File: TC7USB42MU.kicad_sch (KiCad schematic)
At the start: 5 parts

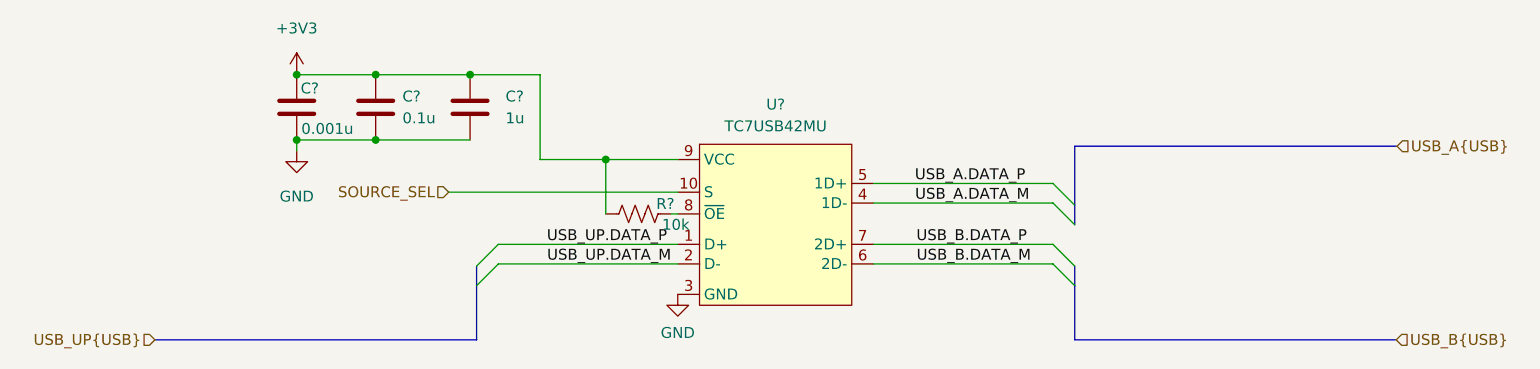
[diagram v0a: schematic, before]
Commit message: Adding 5v and 3v3 buck
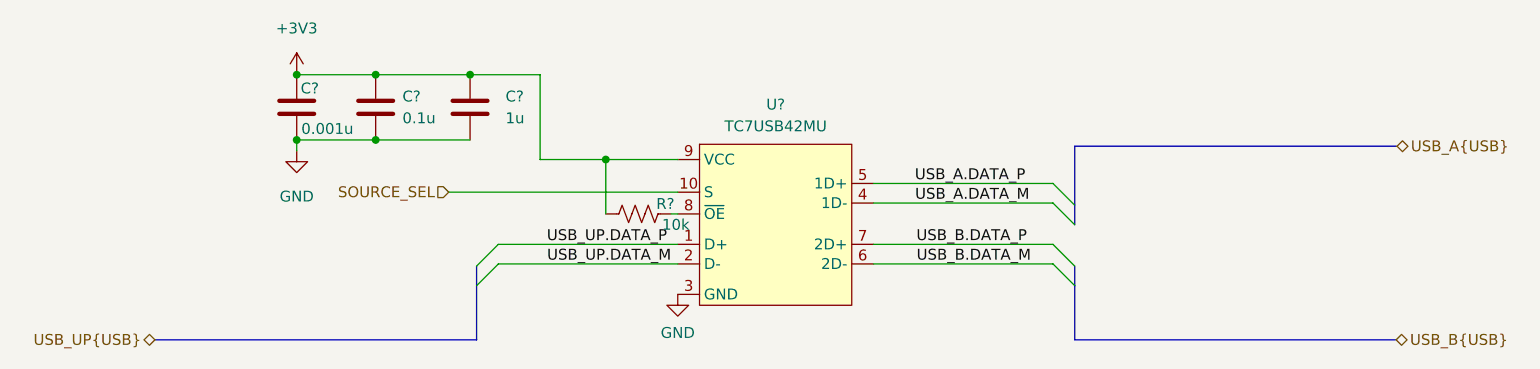
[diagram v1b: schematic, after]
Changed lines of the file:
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@@
     (effects (font (size 1.27 1.27)) (justify right))
   )
-  (hierarchical_label "USB_B{USB}" (shape input) (at 220.0148 104.9528 0)
+  (hierarchical_label "USB_B{USB}" (shape bidirectional) (at 220.0148 104.9528 0)
     (effects (font (size 1.27 1.27)) (justify left))
   )
-  (hierarchical_label "USB_A{USB}" (shape input) (at 220.1164 82.3468 0)
+  (hierarchical_label "USB_A{USB}" (shape bidirectional) (at 220.1164 82.3468 0)
     (effects (font (size 1.27 1.27)) (justify left))
   )
-  (hierarchical_label "USB_UP{USB}" (shape input) (at 75.057 104.9528 180)
+  (hierarchical_label "USB_UP{USB}" (shape bidirectional) (at 75.057 104.9528 180)
     (effects (font (size 1.27 1.27)) (justify right))
   )

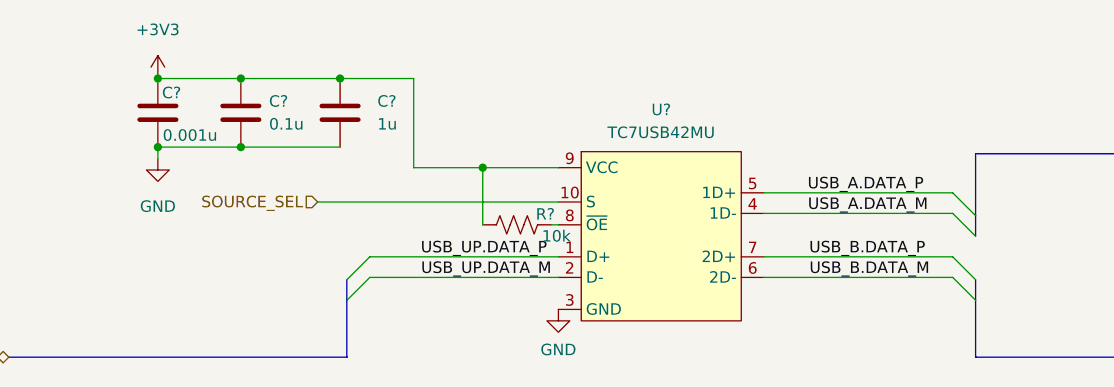
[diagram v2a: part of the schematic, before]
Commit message: Fixing ERC
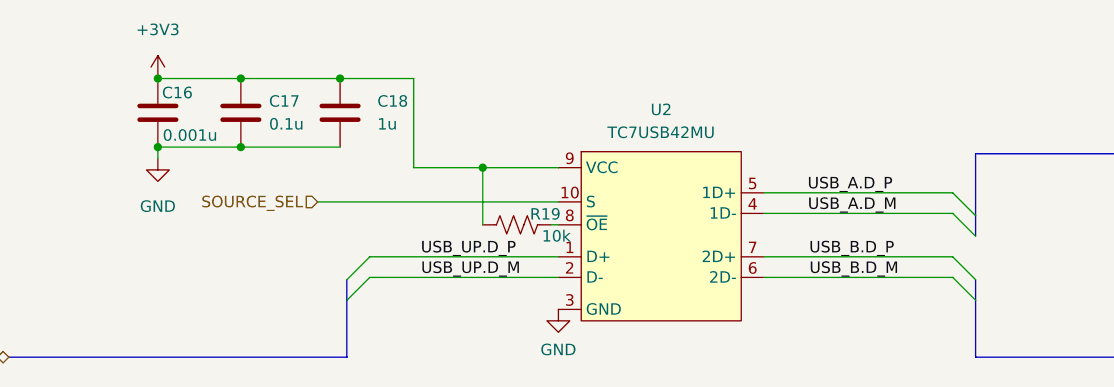
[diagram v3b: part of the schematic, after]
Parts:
- gave numbers to parts that had none: 5
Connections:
- net USB_A.DATA_M renamed USB_A.D_M
- net USB_A.DATA_P renamed USB_A.D_P
- net USB_B.DATA_M renamed USB_B.D_M
- net USB_B.DATA_P renamed USB_B.D_P
- net USB_UP.DATA_M renamed USB_UP.D_M
- net USB_UP.DATA_P renamed USB_UP.D_P
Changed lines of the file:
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@@
     (stroke (width 0) (type default) (color 0 0 0 0))
   )
-  (label "USB_UP.DATA_P" (at 120.8278 93.8022 0)
+  (label "USB_UP.D_P" (at 120.8278 93.8022 0)
     (effects (font (size 1.27 1.27)) (justify left bottom))
   )
-  (label "USB_B.DATA_M" (at 164.0078 96.0882 0)
+  (label "USB_B.D_M" (at 164.0078 96.0882 0)
     (effects (font (size 1.27 1.27)) (justify left bottom))
   )
-  (label "USB_A.DATA_M" (at 163.83 88.9762 0)
+  (label "USB_A.D_M" (at 163.83 88.9762 0)
     (effects (font (size 1.27 1.27)) (justify left bottom))
   )
-  (label "USB_UP.DATA_M" (at 120.8532 96.0882 0)
+  (label "USB_UP.D_M" (at 120.8532 96.0882 0)
     (effects (font (size 1.27 1.27)) (justify left bottom))
   )
-  (label "USB_B.DATA_P" (at 163.9824 93.8022 0)
+  (label "USB_B.D_P" (at 163.9824 93.8022 0)
     (effects (font (size 1.27 1.27)) (justify left bottom))
   )
-  (label "USB_A.DATA_P" (at 163.8046 86.6902 0)
+  (label "USB_A.D_P" (at 163.8046 86.6902 0)
     (effects (font (size 1.27 1.27)) (justify left bottom))
   )
@@
   (symbol (lib_id "Device:C") (at 100.838 77.8002 0) (unit 1)
     (in_bom yes) (on_board yes) (fields_autoplaced)
-    (property "Reference" "C?" (id 0) (at 103.9622 76.5301 0)
+    (property "Reference" "C17" (id 0) (at 103.9622 76.5301 0)
       (effects (font (size 1.27 1.27)) (justify left))
     )
@@
   (symbol (lib_id "power:GND") (at 136.1186 99.6442 0) (unit 1)
     (in_bom yes) (on_board yes) (fields_autoplaced)
-    (property "Reference" "#PWR?" (id 0) (at 136.1186 105.9942 0)
+    (property "Reference" "#PWR031" (id 0) (at 136.1186 105.9942 0)
       (effects (font (size 1.27 1.27)) hide)
     )
@@
   (symbol (lib_id "Misic:TC7USB42MU") (at 147.8026 93.8022 0) (unit 1)
     (in_bom yes) (on_board yes) (fields_autoplaced)
-    (property "Reference" "U?" (id 0) (at 147.5486 77.47 0))
+    (property "Reference" "U2" (id 0) (at 147.5486 77.47 0))
     (property "Value" "TC7USB42MU" (id 1) (at 147.5486 80.01 0))
     (property "Footprint" "" (id 2) (at 147.2946 94.0562 0)
@@
   (symbol (lib_id "Device:C") (at 111.8616 77.8002 0) (unit 1)
     (in_bom yes) (on_board yes) (fields_autoplaced)
-    (property "Reference" "C?" (id 0) (at 116.0018 76.5301 0)
+    (property "Reference" "C18" (id 0) (at 116.0018 76.5301 0)
       (effects (font (size 1.27 1.27)) (justify left))
     )
@@
   (symbol (lib_id "Device:R_US") (at 131.5212 90.2462 90) (unit 1)
     (in_bom yes) (on_board yes)
-    (property "Reference" "R?" (id 0) (at 134.6708 89.0778 90))
+    (property "Reference" "R19" (id 0) (at 134.6708 89.0778 90))
     (property "Value" "10k" (id 1) (at 135.89 91.5162 90))
     (property "Footprint" "" (id 2) (at 131.7752 89.2302 90)
@@
   (symbol (lib_id "power:GND") (at 91.6178 82.8802 0) (unit 1)
     (in_bom yes) (on_board yes) (fields_autoplaced)
-    (property "Reference" "#PWR?" (id 0) (at 91.6178 89.2302 0)
+    (property "Reference" "#PWR030" (id 0) (at 91.6178 89.2302 0)
       (effects (font (size 1.27 1.27)) hide)
     )
@@
   (symbol (lib_id "power:+3V3") (at 91.6178 73.9902 0) (unit 1)
     (in_bom yes) (on_board yes) (fields_autoplaced)
-    (property "Reference" "#PWR?" (id 0) (at 91.6178 77.8002 0)
+    (property "Reference" "#PWR029" (id 0) (at 91.6178 77.8002 0)
       (effects (font (size 1.27 1.27)) hide)
     )
@@
   (symbol (lib_id "Device:C") (at 91.6178 77.8002 0) (unit 1)
     (in_bom yes) (on_board yes)
-    (property "Reference" "C?" (id 0) (at 92.075 75.5904 0)
+    (property "Reference" "C16" (id 0) (at 92.075 75.5904 0)
       (effects (font (size 1.27 1.27)) (justify left))
     )

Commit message: Pushing what i have now
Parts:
- removed C16: 0.001u, symbol Device:C
- removed C17: 0.1u, symbol Device:C
- removed C18: 1u, symbol Device:C
- removed R19: 10k, symbol Device:R_US
- removed U2: TC7USB42MU, symbol Misic:TC7USB42MU
- added C35: ${Capacitance}, Capacitor_SMD:C_0603_1608Metric_Pad1.08x0.95mm_HandSolder, symbol Rockerrobotics:Capacitors/1276-1034-1-ND
- added C36, C37: ${Capacitance}, Capacitor_SMD:C_0603_1608Metric_Pad1.08x0.95mm_HandSolder, symbol Rockerrobotics:Capacitors/1276-1935-1-ND
- added U6: ${MPN}, Package_SO:MSOP-10_3x3mm_P0.5mm, symbol Rockerrobotics:Integrated Circuits/3565-RS2227XNCT-ND
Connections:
- net GND: now also C35.2, C36.2, C37.2, U6.10 (OE_B), U6.5 (GND)
- net SOURCE_SEL: now also U6.2 (SELECT)
- net USB_A.D_P: now also U6.7 (HSD1_P)
- net USB_B.D_P: now also U6.9 (HSD2_P)
- net USB_UP.D_P: now also U6.3 (D_P)
- new net +5V: C35.1, C36.1, C37.1, U6.1 (V+)
- new net USB_A.D_N: U6.6 (HSD1_N)
- new net USB_B.D_N: U6.8 (HSD2_N)
- new net USB_UP.D_N: U6.4 (D_N)
